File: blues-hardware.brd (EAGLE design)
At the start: 76.7 x 58.2 mm, 3 parts, among them J1 MDT420E01001NOTECARD

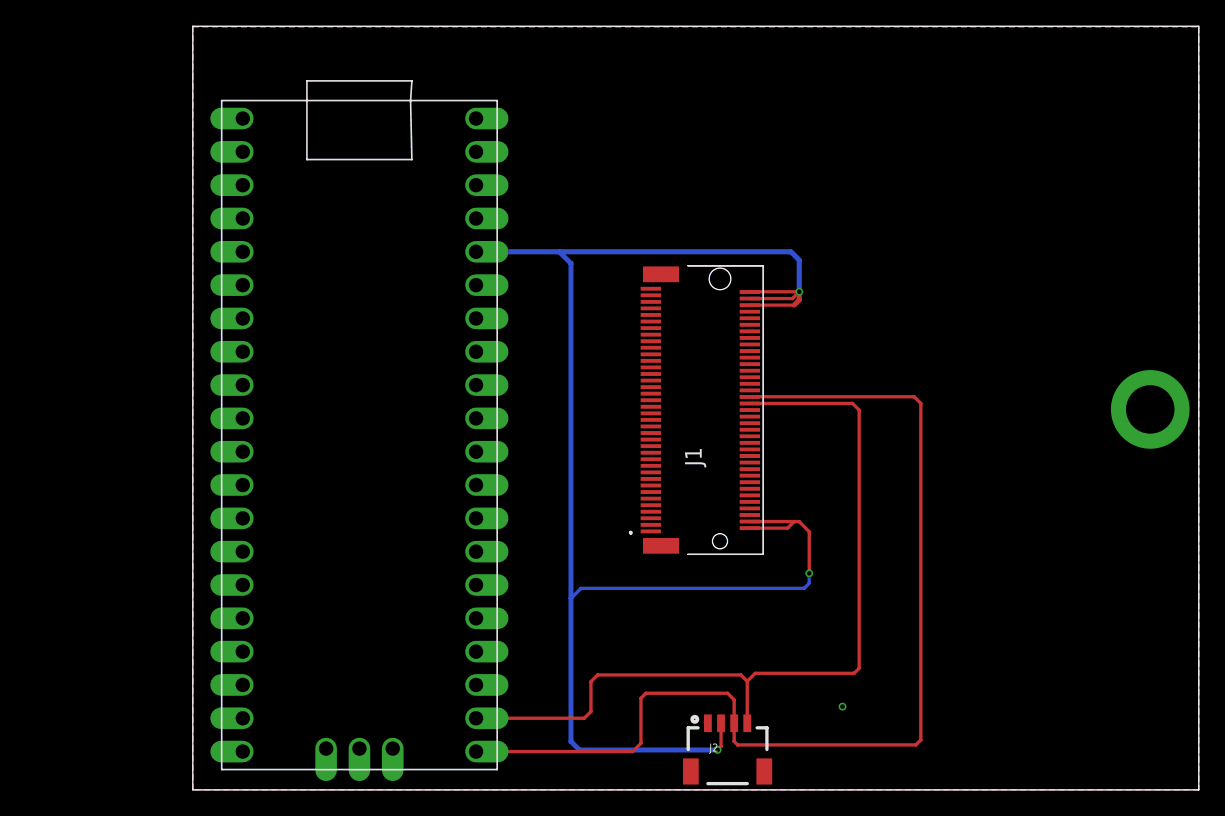
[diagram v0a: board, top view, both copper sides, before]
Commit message: Changes to notecard library
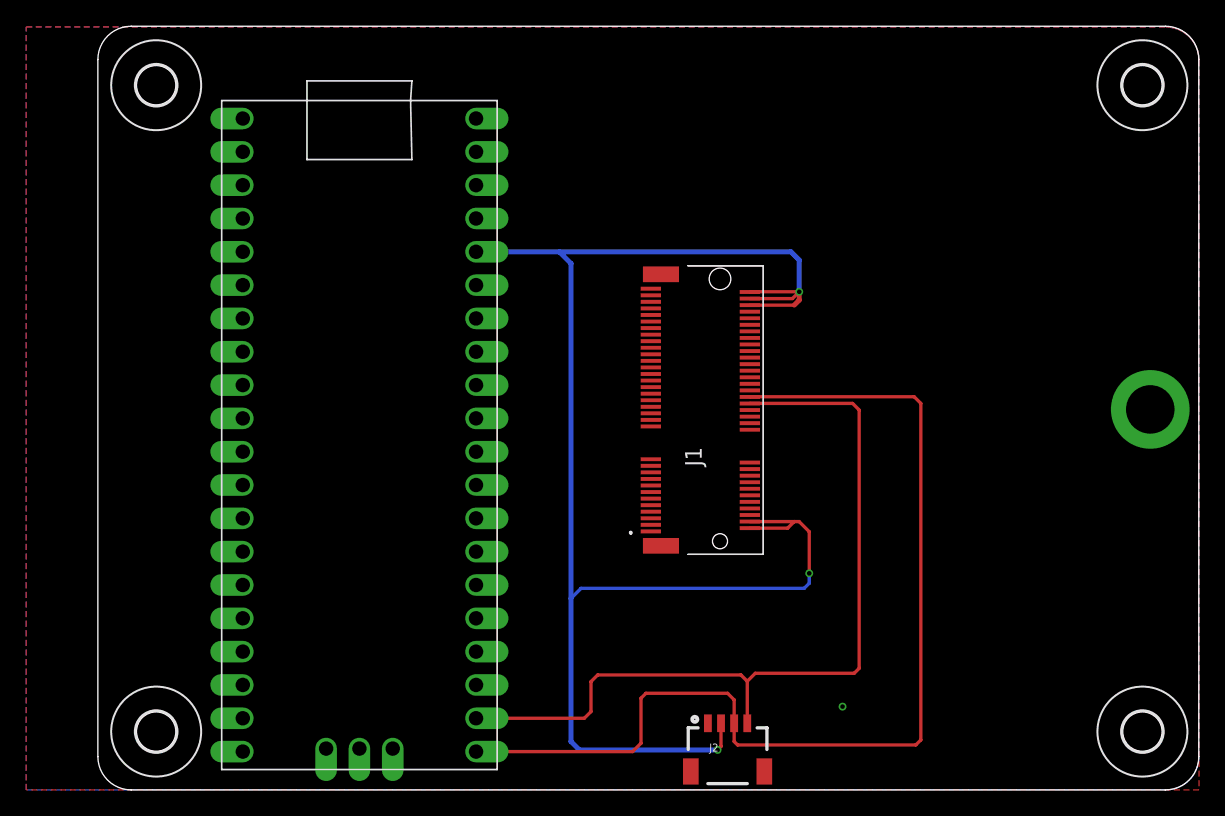
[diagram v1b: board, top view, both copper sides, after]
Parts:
- added H1, H2, H3, H4: MOUNT-HOLE3.0, holes:3,0
- renumbered U$1 to U1
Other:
- board size 76.7 x 58.2 mm -> 83.9 x 58.2 mm
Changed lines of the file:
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@@
 <layer number="115" name="ReferenceISLANDS" color="7" fill="1" visible="no" active="yes"/>
 <layer number="116" name="Patch_BOT" color="9" fill="4" visible="yes" active="yes"/>
+<layer number="117" name="PM_Ref" color="7" fill="1" visible="yes" active="yes"/>
 <layer number="118" name="Rect_Pads" color="7" fill="1" visible="no" active="yes"/>
+<layer number="119" name="PF_Ref" color="7" fill="1" visible="yes" active="yes"/>
+<layer number="120" name="WFL_Ref" color="7" fill="1" visible="yes" active="yes"/>
 <layer number="121" name="_tsilk" color="7" fill="1" visible="yes" active="yes"/>
 <layer number="122" name="_bsilk" color="7" fill="1" visible="yes" active="yes"/>
@@
 <board>
 <plain>
-<wire x1="0" y1="0" x2="76.688" y2="0" width="0" layer="20"/>
-<wire x1="76.688" y1="0" x2="76.688" y2="58.217" width="0" layer="20"/>
-<wire x1="76.688" y1="58.217" x2="0" y2="58.217" width="0" layer="20"/>
-<wire x1="0" y1="58.217" x2="0" y2="0" width="0" layer="20"/>
+<wire x1="-7.239" y1="55.677" x2="-7.239" y2="2.54" width="0" layer="20"/>
+<wire x1="-7.239" y1="2.54" x2="-4.699" y2="0" width="0" layer="20" curve="90"/>
+<wire x1="-4.699" y1="0" x2="74.148" y2="0" width="0" layer="20"/>
+<wire x1="74.148" y1="0" x2="76.688" y2="2.54" width="0" layer="20" curve="90"/>
+<wire x1="76.688" y1="2.54" x2="76.688" y2="55.677" width="0" layer="20"/>
+<wire x1="76.688" y1="55.677" x2="74.148" y2="58.217" width="0" layer="20" curve="90"/>
+<wire x1="74.148" y1="58.217" x2="-4.699" y2="58.217" width="0" layer="20"/>
+<wire x1="-4.699" y1="58.217" x2="-7.239" y2="55.677" width="0" layer="20" curve="90"/>
 </plain>
 <attributes>
@@
 <attribute name="VALUE" x="49.971" y="32.131" size="1.27" layer="27" rot="R90" align="center" display="off"/>
 </element>
-<element name="U$1" library="RaspberryPi_Pico" package="RPI_PICO_TH" value="" x="12.7" y="27.051" smashed="yes"/>
+<element name="U1" library="RaspberryPi_Pico" package="RPI_PICO_TH" value="" x="12.7" y="27.051" smashed="yes"/>
 <element name="J2" library="SparkFun-Connectors" library_urn="urn:adsk.eagle:library:2652347" package="1X04_1MM_RA" package3d_urn="urn:adsk.eagle:package:2652537/1" value="" x="40.767" y="5.08" smashed="yes">
 <attribute name="NAME" x="39.37" y="2.921" size="0.6096" layer="25" font="vector" ratio="20"/>
@@
 <attribute name="VALUE" x="39.116" y="1.778" size="0.6096" layer="27" font="vector" ratio="20"/>
 </element>
+<element name="H1" library="holes" library_urn="urn:adsk.eagle:library:237" package="3,0" package3d_urn="urn:adsk.eagle:package:14277/1" value="MOUNT-HOLE3.0" x="-2.794" y="4.445" smashed="yes">
+<attribute name="POPULARITY" value="3" x="-2.794" y="4.445" size="1.778" layer="27" display="off"/>
+</element>
+<element name="H2" library="holes" library_urn="urn:adsk.eagle:library:237" package="3,0" package3d_urn="urn:adsk.eagle:package:14277/1" value="MOUNT-HOLE3.0" x="72.39" y="4.445" smashed="yes">
+<attribute name="POPULARITY" value="3" x="72.39" y="4.445" size="1.778" layer="27" display="off"/>
+</element>
+<element name="H3" library="holes" library_urn="urn:adsk.eagle:library:237" package="3,0" package3d_urn="urn:adsk.eagle:package:14277/1" value="MOUNT-HOLE3.0" x="72.39" y="53.721" smashed="yes">
+<attribute name="POPULARITY" value="3" x="72.39" y="53.721" size="1.778" layer="27" display="off"/>
+</element>
+<element name="H4" library="holes" library_urn="urn:adsk.eagle:library:237" package="3,0" package3d_urn="urn:adsk.eagle:package:14277/1" value="MOUNT-HOLE3.0" x="-2.794" y="53.721" smashed="yes">
+<attribute name="POPULARITY" value="3" x="-2.794" y="53.721" size="1.778" layer="27" display="off"/>
+</element>
 </elements>
 <signals>
 <signal name="GND">
-<contactref element="J1" pad="MP1"/>
-<contactref element="U$1" pad="GND@1"/>
-<contactref element="U$1" pad="GND@2"/>
-<contactref element="U$1" pad="GND@3"/>
-<contactref element="U$1" pad="GND@4"/>
-<contactref element="U$1" pad="GND@5"/>
-<contactref element="U$1" pad="GND@6"/>
-<contactref element="U$1" pad="GND@7"/>
-<contactref element="U$1" pad="GND@8"/>
+<contactref element="U1" pad="GND@1"/>
+<contactref element="U1" pad="GND@2"/>
+<contactref element="U1" pad="GND@3"/>
+<contactref element="U1" pad="GND@4"/>
+<contactref element="U1" pad="GND@5"/>
+<contactref element="U1" pad="GND@6"/>
+<contactref element="U1" pad="GND@7"/>
+<contactref element="U1" pad="GND@8"/>
 <contactref element="J1" pad="5"/>
 <contactref element="J1" pad="3"/>
@@
 <contactref element="J1" pad="73"/>
 <contactref element="J1" pad="71"/>
+<contactref element="J2" pad="1"/>
+<polygon width="0.1524" layer="1">
+<vertex x="-12.7" y="0"/>
+<vertex x="-12.7" y="58.166"/>
+<vertex x="74.168" y="58.166" curve="-90"/>
+<vertex x="76.708" y="55.626"/>
+<vertex x="76.708" y="0"/>
+</polygon>
+<polygon width="0.1524" layer="16">
+<vertex x="-12.7" y="0"/>
+<vertex x="-12.7" y="58.166"/>
+<vertex x="74.168" y="58.166" curve="-90"/>
+<vertex x="76.708" y="55.626"/>
+<vertex x="76.708" y="2.54" curve="-90"/>
+<vertex x="74.168" y="0"/>
+</polygon>
+<via x="49.53" y="6.35" extent="1-16" drill="0.35"/>
+<contactref element="J1" pad="MP1"/>
 <contactref element="J1" pad="6"/>
 <contactref element="J1" pad="18"/>
 <contactref element="J1" pad="MP2"/>
-<contactref element="J2" pad="1"/>
-<polygon width="0.1524" layer="1">
-<vertex x="0" y="0"/>
-<vertex x="0" y="58.166"/>
-<vertex x="76.708" y="58.166"/>
-<vertex x="76.708" y="0"/>
-</polygon>
-<polygon width="0.1524" layer="16">
-<vertex x="0" y="0"/>
-<vertex x="0" y="58.166"/>
-<vertex x="76.708" y="58.166"/>
-<vertex x="76.708" y="0"/>
-</polygon>
-<via x="49.53" y="6.35" extent="1-16" drill="0.35"/>
 </signal>
 <signal name="3.3V">
-<contactref element="U$1" pad="3V3"/>
+<contactref element="U1" pad="3V3"/>
 <contactref element="J2" pad="2"/>
 <contactref element="J1" pad="74"/>
@@
 </signal>
 <signal name="SDA">
-<contactref element="U$1" pad="GP16"/>
+<contactref element="U1" pad="GP16"/>
 <contactref element="J2" pad="3"/>
 <contactref element="J1" pad="42"/>
@@
 </signal>
 <signal name="SCL">
-<contactref element="U$1" pad="GP17"/>
+<contactref element="U1" pad="GP17"/>
 <contactref element="J2" pad="4"/>
 <contactref element="J1" pad="40"/>
